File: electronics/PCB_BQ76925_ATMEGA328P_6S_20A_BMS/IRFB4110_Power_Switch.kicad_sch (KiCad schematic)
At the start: 8 parts, among them Q1 IRFB4110, Q2 IRFB4110, Q3 IRFB4110, Q4 IRFB4110

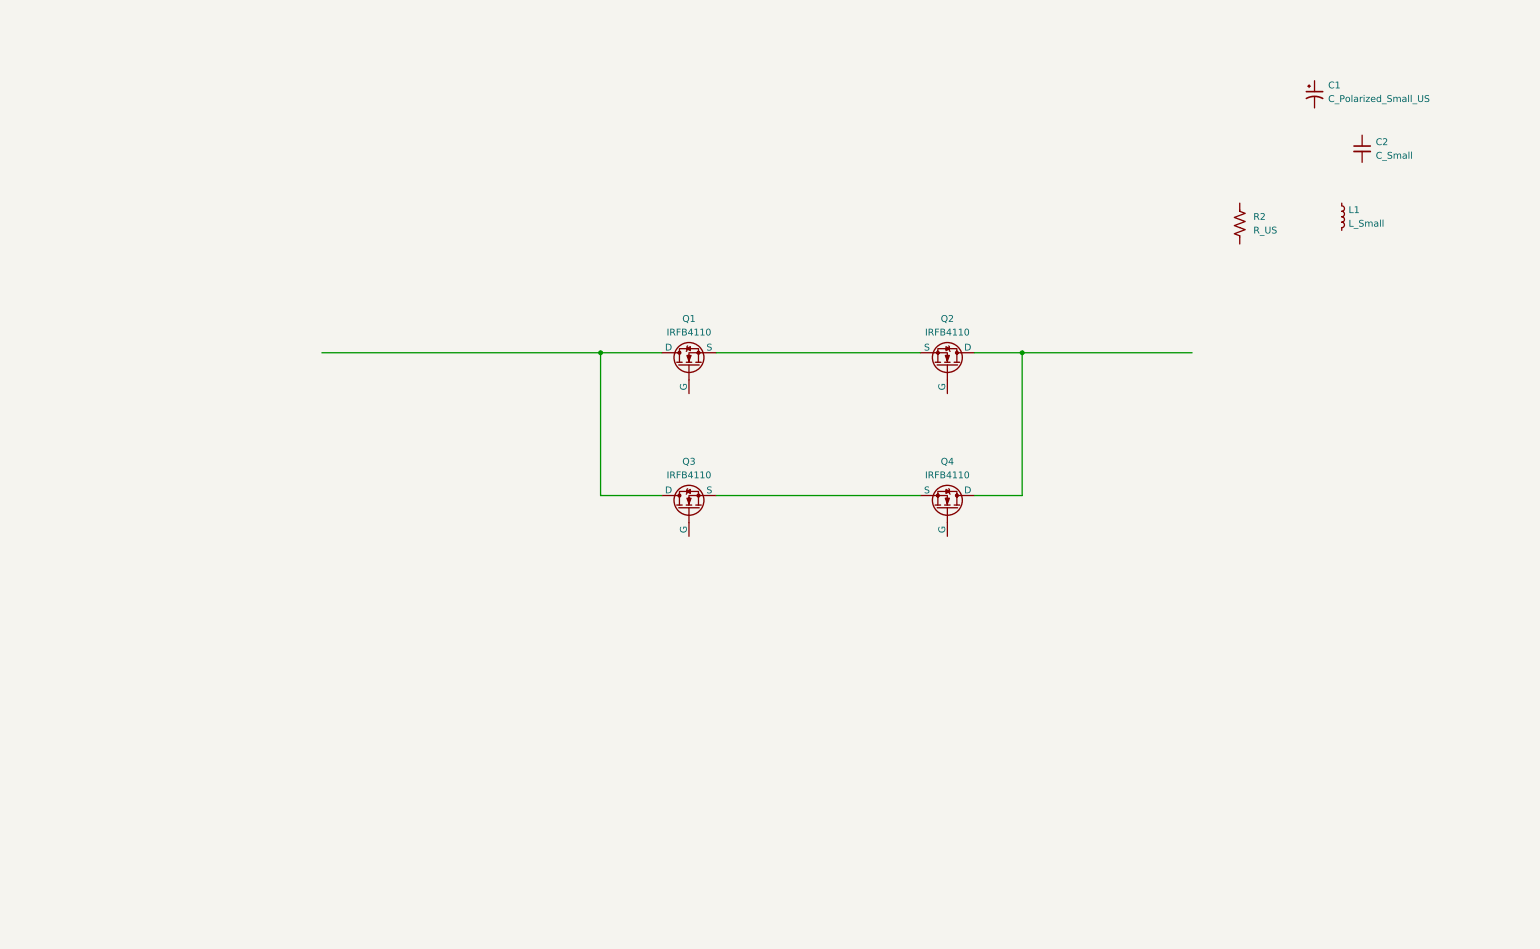
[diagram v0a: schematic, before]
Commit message: schematic completed component need to be finalised
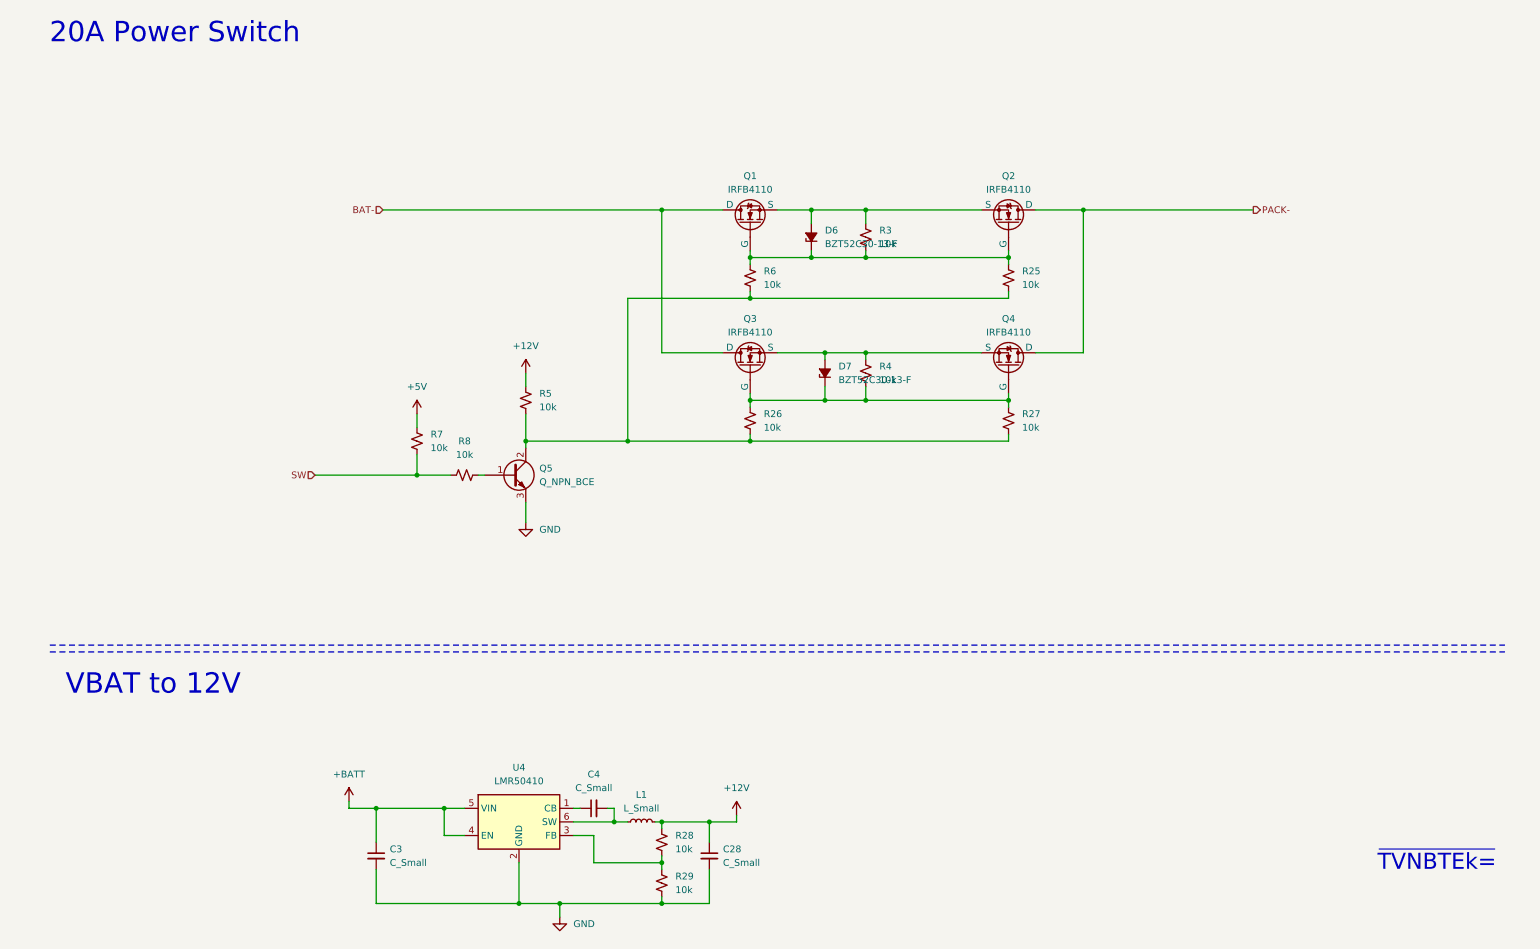
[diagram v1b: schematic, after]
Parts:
- removed C1: C_Polarized_Small_US, symbol BQ76925_ATMEGA328P_6S_20A_BMS:C_Polarized_Small_US
- removed C2: C_Small, symbol BQ76925_ATMEGA328P_6S_20A_BMS:C_Small
- removed R2: R_US, symbol BQ76925_ATMEGA328P_6S_20A_BMS:R_US
- added C28, C3, C4: C_Small, symbol BQ76925_ATMEGA328P_6S_20A_BMS:C_Small
- added D6, D7: BZT52C30-13-F, symbol BQ76925_ATMEGA328P_6S_20A_BMS:D_Zener_Small_Filled
- added Q5: Q_NPN_BCE, symbol BQ76925_ATMEGA328P_6S_20A_BMS:Q_NPN_BCE
- added R25, R26, R27, R28, R29, R3, R4, R5, R6, R7, R8: 10k, symbol BQ76925_ATMEGA328P_6S_20A_BMS:R_Small_US
- added U4: LMR50410, Package_TO_SOT_SMD:SOT-23-6, symbol BQ76925_ATMEGA328P_6S_20A_BMS:LMR50410
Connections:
- net at Q1.1 (G): now also Q2.1 (G), D6.1 (K), R25.1, R3.1, R6.1
- net BAT-: now reaches Q1.2 (D), Q3.2 (D)
- net at Q1.3 (S), Q2.3 (S): now also D6.2 (A), R3.2
- net PACK-: now reaches Q2.2 (D), Q4.2 (D)
- net at L1.1: now also C4.2, U4.6 (SW)
- net +12V: now reaches L1.2
- net +12V: now also C28.1, R28.1, R5.2
- net at Q4.1 (G): now also Q3.1 (G), D7.1 (K), R26.1, R27.1, R4.1
- net at Q3.3 (S), Q4.3 (S): now also D7.2 (A), R4.2
- new net: Q5.2 (C), R25.2, R26.2, R27.2, R5.1, R6.2
- new net: C4.1, U4.1 (CB)
- new net: R28.2, R29.1, U4.3 (FB)
- new net: Q5.1 (B), R8.1
- new net +5V: R7.2
- new net +BATT: C3.1, U4.4 (EN), U4.5 (VIN)
- new net GND: C28.2, C3.2, Q5.3 (E), R29.2, U4.2 (GND)
- new net SW: R7.1, R8.2
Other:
- note added: "20A Power Switch"
- note added: "VBAT to 12V"
- note added: "~{TVNBTEk=}"
- company: (none) -> M S Ali
- title: (none) -> Raven-I Sentinel
- moved on the sheet: L1, Q1, Q2, Q3, Q4

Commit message: Schematic completed components calculated need to check avaialability
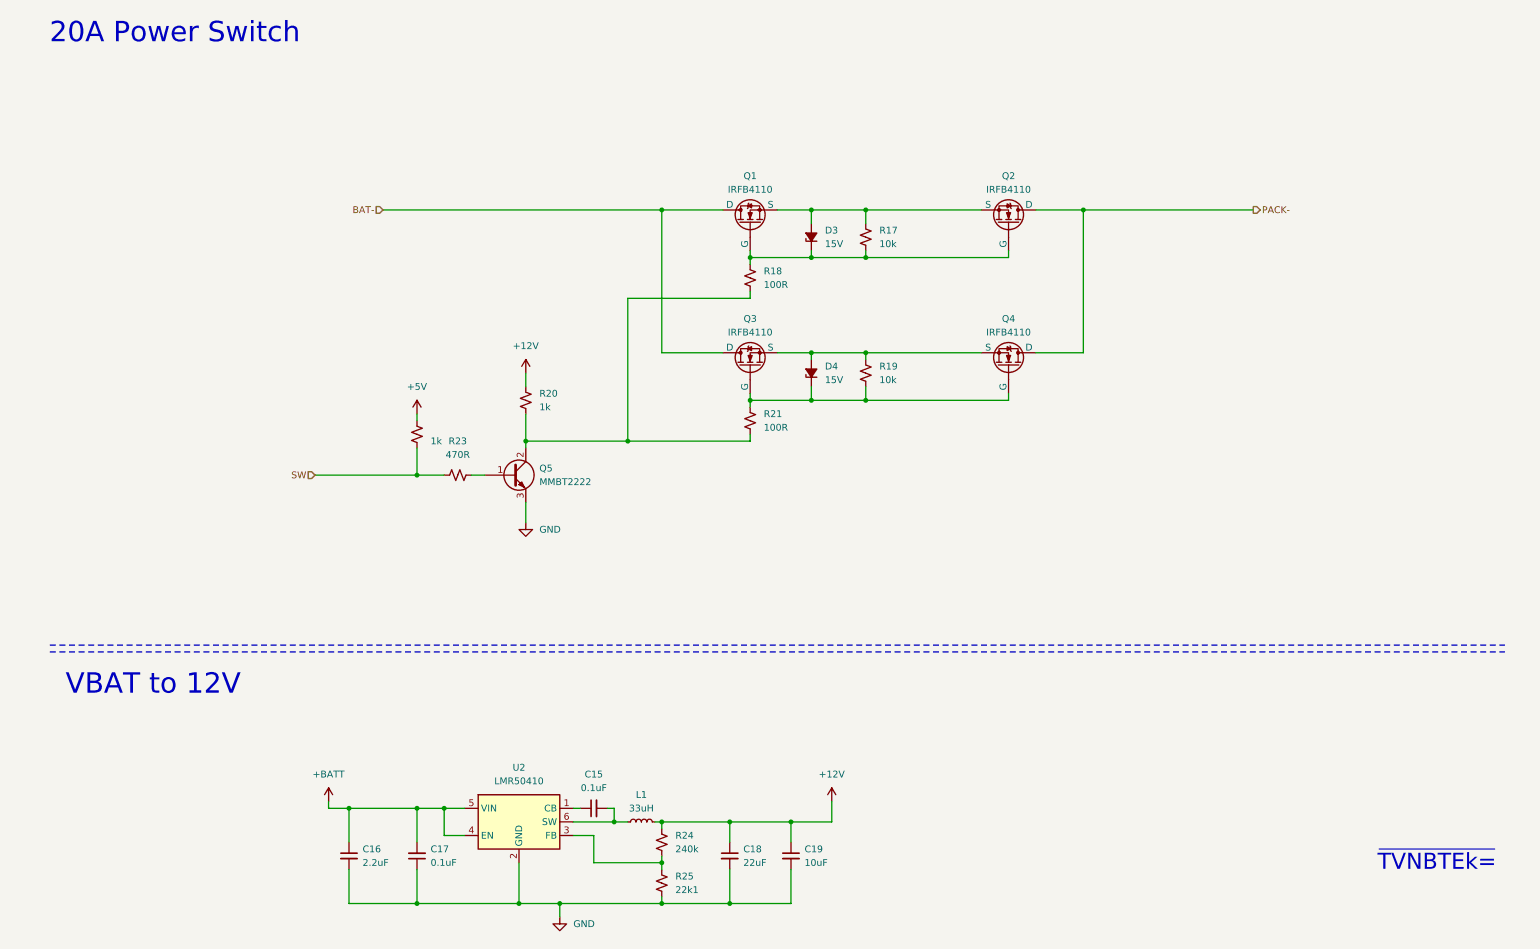
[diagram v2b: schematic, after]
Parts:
- removed R25, R27: 10k, symbol BQ76925_ATMEGA328P_6S_20A_BMS:R_Small_US
- added C17: 0.1uF, symbol BQ76925_ATMEGA328P_6S_20A_BMS:C_Small
- added C19: 10uF, symbol BQ76925_ATMEGA328P_6S_20A_BMS:C_Small
- C15: renamed from C4; value C_Small -> 0.1uF
- C16: renamed from C3; value C_Small -> 2.2uF
- C18: renamed from C28; value C_Small -> 22uF
- D3: renamed from D6; value BZT52C30-13-F -> 15V
- D4: renamed from D7; value BZT52C30-13-F -> 15V
- L1: value L_Small -> 33uH
- Q5: value Q_NPN_BCE -> MMBT2222
- R17: renamed from R3; footprint (none) -> Resistor_SMD:R_0603_1608Metric_Pad0.98x0.95mm_HandSolder
- R18: renamed from R6; value 10k -> 100R; footprint (none) -> Resistor_SMD:R_0603_1608Metric_Pad0.98x0.95mm_HandSolder
- R19: renamed from R4; footprint (none) -> Resistor_SMD:R_0603_1608Metric_Pad0.98x0.95mm_HandSolder
- R20: renamed from R5; value 10k -> 1k; footprint (none) -> Resistor_SMD:R_0603_1608Metric_Pad0.98x0.95mm_HandSolder
- R21: renamed from R26; value 10k -> 100R; footprint (none) -> Resistor_SMD:R_0603_1608Metric_Pad0.98x0.95mm_HandSolder
- R22: renamed from R7; value 10k -> 1k; footprint (none) -> Resistor_SMD:R_0603_1608Metric_Pad0.98x0.95mm_HandSolder
- R23: renamed from R8; value 10k -> 470R; footprint (none) -> Resistor_SMD:R_0603_1608Metric_Pad0.98x0.95mm_HandSolder
- R24: renamed from R28; value 10k -> 240k; footprint (none) -> Resistor_SMD:R_0603_1608Metric_Pad0.98x0.95mm_HandSolder
- R25: renamed from R29; value 10k -> 22k1; footprint (none) -> Resistor_SMD:R_0603_1608Metric_Pad0.98x0.95mm_HandSolder
- renumbered U4 to U2
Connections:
- net +12V: now also C19.1
- net +BATT: now also C17.2
- net GND: now also C17.1, C19.2
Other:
- moved on the sheet: C16, C18, D4, R23

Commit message: added power led and mcu test led in schematic
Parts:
- added D5: LED, symbol Device:LED_Small_Filled
- added R27: 1k, Resistor_SMD:R_0603_1608Metric_Pad0.98x0.95mm_HandSolder, symbol BQ76925_ATMEGA328P_6S_20A_BMS:R_Small_US
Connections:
- net +12V: now also R27.1
- net GND: now also D5.1 (K)
- new net: D5.2 (A), R27.2
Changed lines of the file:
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@@
+	)
+	(junction
+		(at 151.13 181.61)
+		(diameter 0)
+		(color 0 0 0 0)
 	)
 	(junction
@@
 	)
 	(junction
+		(at 161.29 166.37)
+		(diameter 0)
+		(color 0 0 0 0)
+	)
+	(junction
 		(at 86.36 163.83)
 		(diameter 0)
@@
 	(wire
 		(pts
+			(xy 161.29 181.61) (xy 151.13 181.61)
+		)
+		(stroke
+			(width 0)
+			(type default)
+		)
+	)
+	(wire
+		(pts
 			(xy 165.1 78.74) (xy 165.1 80.01)
 		)
@@
 	(wire
 		(pts
-			(xy 158.75 166.37) (xy 151.13 166.37)
+			(xy 165.1 166.37) (xy 161.29 166.37)
 		)
 		(stroke
@@
 	(wire
 		(pts
+			(xy 161.29 179.07) (xy 161.29 181.61)
+		)
+		(stroke
+			(width 0)
+			(type default)
+		)
+	)
+	(wire
+		(pts
 			(xy 165.1 85.09) (xy 165.1 87.63)
 		)
@@
 	(wire
 		(pts
-			(xy 158.75 162.56) (xy 158.75 166.37)
+			(xy 165.1 162.56) (xy 165.1 166.37)
 		)
 		(stroke
@@
 		)
 	)
+	(wire
+		(pts
+			(xy 161.29 166.37) (xy 161.29 168.91)
+		)
+		(stroke
+			(width 0)
+			(type default)
+		)
+	)
 	(polyline
 		(pts
@@
 		(pts
 			(xy 100.33 173.99) (xy 100.33 181.61)
+		)
+		(stroke
+			(width 0)
+			(type default)
+		)
+	)
+	(wire
+		(pts
+			(xy 161.29 166.37) (xy 151.13 166.37)
 		)
 		(stroke
@@
 	(symbol
 		(lib_id "BQ76925_ATMEGA328P_6S_20A_BMS:+12V")
-		(at 158.75 162.56 0)
+		(at 165.1 162.56 0)
 		(unit 1)
 		(exclude_from_sim no)
@@
 		(fields_autoplaced yes)
 		(property "Reference" "#PWR024"
-			(at 158.75 166.37 0)
+			(at 165.1 166.37 0)
 			(effects
 				(font
@@
 		)
 		(property "Value" "+12V"
-			(at 158.75 157.48 0)
+			(at 165.1 157.48 0)
 			(effects
 				(font
@@
 		)
 		(property "Footprint" ""
-			(at 158.75 162.56 0)
+			(at 165.1 162.56 0)
 			(effects
 				(font
@@
 		)
 		(property "Datasheet" ""
-			(at 158.75 162.56 0)
+			(at 165.1 162.56 0)
 			(effects
 				(font
@@
 		)
 		(property "Description" "Power symbol creates a global label with name \"+12V\""
-			(at 158.75 162.56 0)
+			(at 165.1 162.56 0)
 			(effects
 				(font
@@
 				(path "/624a087f-322b-4a70-8c29-0e4f8f018e16/8ac54c25-c4c2-47e9-9217-d0c10d04e631"
 					(reference "#PWR021")
+					(unit 1)
+				)
+			)
+		)
+	)
+	(symbol
+		(lib_id "BQ76925_ATMEGA328P_6S_20A_BMS:R_Small_US")
+		(at 161.29 171.45 0)
+		(unit 1)
+		(exclude_from_sim no)
+		(in_bom yes)
+		(on_board yes)
+		(dnp no)
+		(fields_autoplaced yes)
+		(property "Reference" "R27"
+			(at 163.83 170.1799 0)
+			(effects
+				(font
+					(size 1.27 1.27)
+				)
+				(justify left)
+			)
+		)
+		(property "Value" "1k"
+			(at 163.83 172.7199 0)
+			(effects
+				(font
+					(size 1.27 1.27)
+				)
+				(justify left)
+			)
+		)
+		(property "Footprint" "Resistor_SMD:R_0603_1608Metric_Pad0.98x0.95mm_HandSolder"
+			(at 161.29 171.45 0)
+			(effects
+				(font
+					(size 1.27 1.27)
+				)
+				(hide yes)
+			)
+		)
+		(property "Datasheet" "~"
+			(at 161.29 171.45 0)
+			(effects
+				(font
+					(size 1.27 1.27)
+				)
+				(hide yes)
+			)
+		)
+		(property "Description" "Resistor, small US symbol"
+			(at 161.29 171.45 0)
+			(effects
+				(font
+					(size 1.27 1.27)
+				)
+				(hide yes)
+			)
+		)
+		(pin "1"
+		)
+		(pin "2"
+		)
+		(instances
+			(project "BQ76925_ATMEGA328P_6S_20A_BMS"
+				(path "/624a087f-322b-4a70-8c29-0e4f8f018e16/8ac54c25-c4c2-47e9-9217-d0c10d04e631"
+					(reference "R27")
 					(unit 1)
 				)
@@
 					(unit 1)
 				)
+			)
+		)
+	)
+	(symbol
+		(lib_id "Device:LED_Small_Filled")
+		(at 161.29 176.53 90)
+		(unit 1)
+		(exclude_from_sim no)
+		(in_bom yes)
+		(on_board yes)
+		(dnp no)
+		(fields_autoplaced yes)
+		(property "Reference" "D5"
+			(at 163.83 175.1964 90)
+			(effects
+				(font
+					(size 1.27 1.27)
+				)
+				(justify right)
+			)
+		)
+		(property "Value" "LED"
+			(at 163.83 177.7364 90)
+			(effects
+				(font
+					(size 1.27 1.27)
+				)
+				(justify right)
+			)
+		)
+		(property "Footprint" ""
+			(at 161.29 176.53 90)
+			(effects
+				(font
+					(size 1.27 1.27)
+				)
+				(hide yes)
+			)
+		)
+		(property "Datasheet" "~"
+			(at 161.29 176.53 90)
+			(effects
+				(font
+					(size 1.27 1.27)
+				)
+				(hide yes)
+			)
+		)
+		(property "Description" "Light emitting diode, small symbol, filled shape"
+			(at 161.29 176.53 0)
+			(effects
+				(font
+					(size 1.27 1.27)
+				)
+				(hide yes)
+			)
+		)
+		(pin "1"
+		)
+		(pin "2"
+		)
+		(instances
+			(project "BQ76925_ATMEGA328P_6S_20A_BMS"
+				(path "/624a087f-322b-4a70-8c29-0e4f8f018e16/8ac54c25-c4c2-47e9-9217-d0c10d04e631"
+					(reference "D5")
+					(unit 1)
+				)

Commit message: common footprints assigned to symbols
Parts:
- C15, C17: value 0.1uF -> 100nF/50V; footprint (none) -> Capacitor_SMD:C_0805_2012Metric_Pad1.18x1.45mm_HandSolder
- C18: value 22uF -> 22uF/35V; footprint (none) -> Capacitor_SMD:CP_Elec_6.3x5.7
- C19: value 10uF -> 10uF/16V; footprint (none) -> Capacitor_SMD:C_0603_1608Metric_Pad1.08x0.95mm_HandSolder
- D5: footprint (none) -> Resistor_SMD:R_0805_2012Metric_Pad1.20x1.40mm_HandSolder
- L1: value 33uH -> 100uH; footprint (none) -> Inductor_SMD:L_7.3x7.3_H3.5
- Q5: value MMBT2222 -> BC817; footprint (none) -> Package_TO_SOT_SMD:SOT-23
- R18, R21: footprint Resistor_SMD:R_0603_1608Metric_Pad0.98x0.95mm_HandSolder -> Resistor_SMD:R_1206_3216Metric_Pad1.30x1.75mm_HandSolder
- R24: footprint Resistor_SMD:R_0603_1608Metric_Pad0.98x0.95mm_HandSolder -> Resistor_SMD:R_0805_2012Metric_Pad1.20x1.40mm_HandSolder
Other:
- note added: "270k"
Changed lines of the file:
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@@
+		)
+	)
+	(text "270k"
+		(exclude_from_sim no)
+		(at 132.08 165.354 0)
+		(effects
+			(font
+				(size 1.27 1.27)
+			)
 		)
 	)
@@
 			)
 		)
-		(property "Value" "0.1uF"
+		(property "Value" "100nF/50V"
 			(at 83.82 173.9835 0)
 			(effects
@@
 			)
 		)
-		(property "Footprint" ""
+		(property "Footprint" "Capacitor_SMD:C_0805_2012Metric_Pad1.18x1.45mm_HandSolder"
 			(at 81.28 172.72 0)
 			(effects
@@
 			)
 		)
-		(property "Value" "0.1uF"
+		(property "Value" "100nF/50V"
 			(at 114.3063 160.02 90)
 			(effects
@@
 			)
 		)
-		(property "Footprint" ""
+		(property "Footprint" "Capacitor_SMD:C_0805_2012Metric_Pad1.18x1.45mm_HandSolder"
 			(at 114.3 163.83 0)
 			(effects
@@
 			)
 		)
-		(property "Footprint" "Resistor_SMD:R_0603_1608Metric_Pad0.98x0.95mm_HandSolder"
+		(property "Footprint" "Resistor_SMD:R_0805_2012Metric_Pad1.20x1.40mm_HandSolder"
 			(at 127 170.18 0)
 			(effects
@@
 			)
 		)
-		(property "Value" "10uF"
+		(property "Value" "10uF/16V"
 			(at 153.67 173.9962 0)
 			(effects
@@
 			)
 		)
-		(property "Footprint" ""
+		(property "Footprint" "Capacitor_SMD:C_0603_1608Metric_Pad1.08x0.95mm_HandSolder"
 			(at 151.13 172.72 0)
 			(effects
@@
 			)
 		)
-		(property "Value" "MMBT2222"
+		(property "Value" "BC817"
 			(at 104.14 102.8699 0)
 			(effects
@@
 			)
 		)
-		(property "Footprint" ""
+		(property "Footprint" "Package_TO_SOT_SMD:SOT-23"
 			(at 104.14 99.06 0)
 			(effects
@@
 			)
 		)
-		(property "Footprint" "Resistor_SMD:R_0603_1608Metric_Pad0.98x0.95mm_HandSolder"
+		(property "Footprint" "Resistor_SMD:R_1206_3216Metric_Pad1.30x1.75mm_HandSolder"
 			(at 143.51 91.44 0)
 			(effects
@@
 			)
 		)
-		(property "Value" "22uF"
+		(property "Value" "22uF/35V"
 			(at 142.24 173.9962 0)
 			(effects
@@
 			)
 		)
-		(property "Footprint" ""
+		(property "Footprint" "Capacitor_SMD:CP_Elec_6.3x5.7"
 			(at 139.7 172.72 0)
 			(effects
@@
 			)
 		)
-		(property "Value" "33uH"
+		(property "Value" "100uH"
 			(at 123.19 163.83 90)
 			(effects
@@
 			)
 		)
-		(property "Footprint" ""
+		(property "Footprint" "Inductor_SMD:L_7.3x7.3_H3.5"
 			(at 123.19 166.37 0)
 			(effects
@@
 			)
 		)
-		(property "Footprint" ""
+		(property "Footprint" "Resistor_SMD:R_0805_2012Metric_Pad1.20x1.40mm_HandSolder"
 			(at 161.29 176.53 90)
 			(effects
@@
 			)
 		)
-		(property "Footprint" "Resistor_SMD:R_0603_1608Metric_Pad0.98x0.95mm_HandSolder"
+		(property "Footprint" "Resistor_SMD:R_1206_3216Metric_Pad1.30x1.75mm_HandSolder"
 			(at 143.51 64.77 0)
 			(effects
